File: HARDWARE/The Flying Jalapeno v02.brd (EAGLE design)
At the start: 73.7 x 72.4 mm, 100 parts, among them Q2 MMBT2222A, Q3 NDP6020P, Q4 MMBT2222A, Q5 NDP6020P, Q6 BSS138, 200mA/50V, Q7 BSS138, 200mA/50V, U1 ATMEGA2560AU, U2 LM1117, U3 LM1117, U4 LM1117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

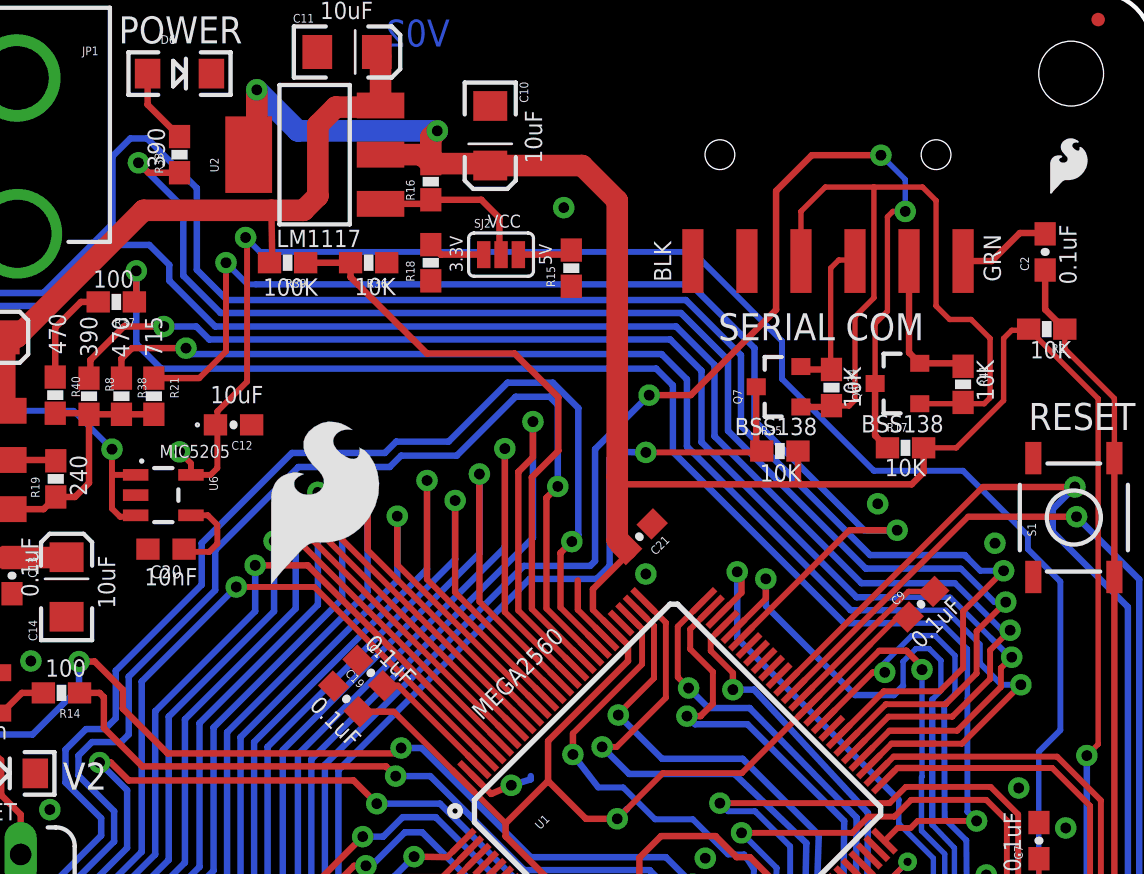
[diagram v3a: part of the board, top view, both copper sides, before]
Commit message: removed RAW split test, moved pwr led from io to VCC
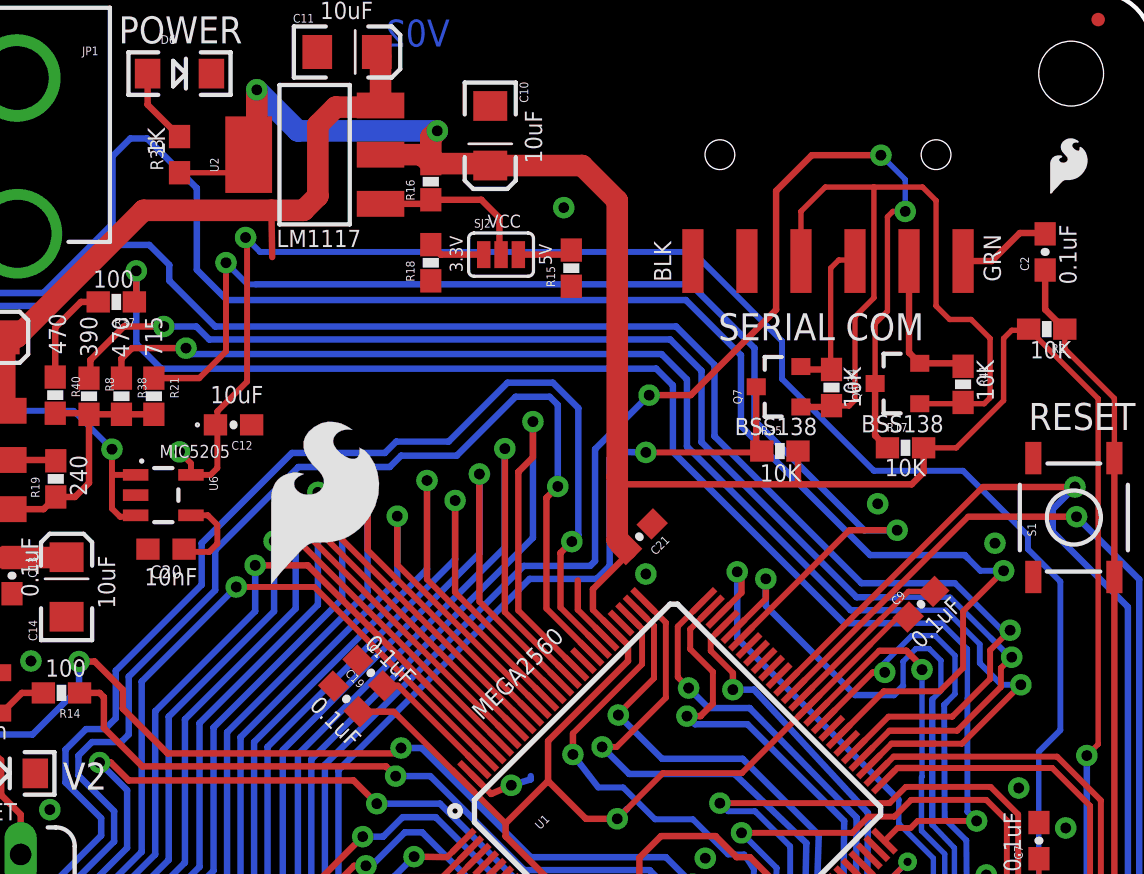
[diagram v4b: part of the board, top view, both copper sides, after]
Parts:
- removed R36: 10K, SparkFun-Resistors:0603-RES
- removed R39: 100k, SparkFun-Resistors:0603-RES
- R33: value 390 -> 1k; device SparkFun-Resistors:0603-RES -> SparkFun-Resistors:0603
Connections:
- removed net 34/RAW_PASS_LED: R33.1, U1.56
- net A13/RAW_READ: no longer R36.2, R39.1
- net GND: no longer R36.1
- net RAW: no longer R39.2
- net VCC: now also R33.1
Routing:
- net 34/RAW_PASS_LED: track 66.7 -> 0.00 mm, vias 2 -> 0
- net A13/RAW_READ: track 28.8 -> 0.00 mm
- net VCC: track 187.9 -> 191.5 mm
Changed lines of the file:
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@@
 <text x="1.6256" y="39.9542" size="0.8128" layer="21" font="vector" ratio="15">10K</text>
 <text x="13.8684" y="40.132" size="0.8128" layer="21" font="vector" ratio="15">10K</text>
-<text x="38.1" y="58.9788" size="0.8128" layer="21" font="vector" ratio="15" rot="R180">10K</text>
 <text x="12.1666" y="40.7416" size="0.8128" layer="21" font="vector" ratio="15" rot="R180">100</text>
 <text x="23.5458" y="41.0464" size="0.8128" layer="21" font="vector" ratio="15" rot="R180">100</text>
@@
 <text x="44.9834" y="64.3636" size="0.8128" layer="21" font="vector" ratio="15" rot="R90">10uF</text>
 <text x="37.0332" y="71.9582" size="0.8128" layer="21" font="vector" ratio="15" rot="R180">10uF</text>
-<text x="34.4424" y="58.9534" size="0.8128" layer="21" font="vector" ratio="15" rot="R180">100K</text>
-<text x="26.4414" y="66.04" size="0.8128" layer="21" font="vector" ratio="15" rot="R270">390</text>
+<text x="26.4414" y="66.04" size="0.8128" layer="21" font="vector" ratio="15" rot="R270">1K</text>
 <text x="36.4744" y="61.2394" size="0.8128" layer="21" font="vector" ratio="15" rot="R180">LM1117</text>
 <text x="6.8326" y="46.609" size="0.8128" layer="21" font="vector" ratio="15" rot="R180">LM1117</text>
@@
 <element name="STANDOFF3" library="SparkFun-Electromechanical" package="STAND-OFF-TIGHT" value="STAND-OFFTIGHT" x="69.85" y="68.58"/>
 <element name="STANDOFF4" library="SparkFun-Electromechanical" package="STAND-OFF-TIGHT" value="STAND-OFFTIGHT" x="3.81" y="68.58"/>
-<element name="R36" library="SparkFun-Resistors" package="0603-RES" value="10K" x="36.83" y="59.69" rot="R180">
-<attribute name="PROD_ID" value="RES-00824" x="36.83" y="59.69" size="1.778" layer="27" font="vector" ratio="15" rot="R180" display="off"/>
-</element>
 <element name="R37" library="SparkFun-Resistors" package="0603-RES" value="100" x="24.9682" y="57.8485" rot="R180">
 <attribute name="PROD_ID" value="RES-07863" x="24.9682" y="57.8485" size="1.778" layer="27" font="vector" ratio="15" rot="R180" display="off"/>
@@
 <attribute name="PROD_ID" value="RES-07869" x="25.2095" y="53.4162" size="1.778" layer="27" font="vector" ratio="15" rot="R270" display="off"/>
 </element>
-<element name="R39" library="SparkFun-Resistors" package="0603-RES" value="100k" x="33.02" y="59.69" rot="R180">
-<attribute name="PROD_ID" value="RES-07828" x="33.02" y="59.69" size="1.778" layer="27" font="vector" ratio="15" rot="R180" display="off"/>
-</element>
 <element name="C19" library="SparkFun-Capacitors" package="0603-CAP" value="0.1uF" x="35.782703125" y="39.187578125" rot="R315">
 <attribute name="PROD_ID" value="CAP-00810" x="35.782703125" y="39.187578125" size="1.778" layer="27" font="vector" ratio="15" rot="R315" display="off"/>
@@
 <attribute name="PROD_ID" value="DIO-00809" x="27.94" y="68.58" size="1.778" layer="27" font="vector" ratio="15" display="off"/>
 </element>
-<element name="R33" library="SparkFun-Resistors" package="0603-RES" value="390" x="27.94" y="64.77" rot="R90">
-<attribute name="PROD_ID" value="RES-07864" x="27.94" y="64.77" size="1.778" layer="27" font="vector" ratio="15" rot="R90" display="off"/>
+<element name="R33" library="SparkFun-Resistors" package="0603" value="1k" x="27.94" y="64.77" rot="R90">
+<attribute name="PROD_ID" value="RES-07856" x="27.94" y="64.77" size="1.778" layer="27" font="vector" ratio="15" rot="R90" display="off"/>
 </element>
 <element name="Q6" library="SparkFun-DiscreteSemi" package="SOT23-3" value="BSS138, 200mA/50V" x="61.7347" y="54.0131" rot="R90">
@@
 <contactref element="JP4" pad="31"/>
 <contactref element="JP4" pad="1"/>
-<contactref element="R36" pad="1"/>
 <contactref element="D3" pad="C"/>
 <contactref element="Y1" pad="2"/>
@@
 <wire x1="63.2714" y1="27.9654" x2="63.2714" y2="25.923240625" width="0.254" layer="1"/>
 <wire x1="63.2714" y1="25.923240625" x2="64.137540625" y2="25.0571" width="0.254" layer="1"/>
+<contactref element="R33" pad="1"/>
+<wire x1="31.191" y1="64.77" x2="30.341" y2="63.92" width="0.254" layer="1"/>
+<wire x1="30.341" y1="63.92" x2="27.94" y2="63.92" width="0.254" layer="1"/>
 </signal>
 <signal name="RAW" class="1">
@@
 <contactref element="SJ3" pad="1"/>
 <contactref element="SJ4" pad="1"/>
-<contactref element="R39" pad="2"/>
 <wire x1="2.032" y1="58.036" x2="4.448" y2="58.036" width="1.016" layer="1"/>
 <wire x1="4.448" y1="58.036" x2="5.6769" y2="56.8071" width="1.016" layer="1"/>
@@
 <via x="16.0909" y="52.7304" extent="1-16" drill="0.508"/>
 <wire x1="16.0909" y1="52.7304" x2="19.6342" y2="52.7304" width="1.016" layer="1"/>
-<wire x1="32.17" y1="59.69" x2="32.297" y2="59.9558" width="0.3048" layer="1"/>
 <wire x1="32.297" y1="59.9558" x2="32.258" y2="62.1538" width="0.3048" layer="1"/>
 <wire x1="3.8354" y1="45.5676" x2="3.8354" y2="44.2468" width="1.016" layer="1"/>
@@
 <signal name="A13/RAW_READ">
 <contactref element="U1" pad="84"/>
-<contactref element="R36" pad="2"/>
-<contactref element="R39" pad="1"/>
-<wire x1="35.98" y1="59.69" x2="33.87" y2="59.69" width="0.3048" layer="1"/>
-<wire x1="46.929328125" y1="40.989090625" x2="44.5008" y2="43.41761875" width="0.2794" layer="1"/>
-<wire x1="44.5008" y1="43.41761875" x2="44.5008" y2="49.6062" width="0.3048" layer="1"/>
-<wire x1="44.5008" y1="49.6062" x2="45.7454" y2="50.8508" width="0.3048" layer="1"/>
-<wire x1="45.7454" y1="50.8508" x2="45.7454" y2="53.3654" width="0.3048" layer="1"/>
-<wire x1="45.7454" y1="53.3654" x2="43.688" y2="55.4228" width="0.3048" layer="1"/>
-<wire x1="43.688" y1="55.4228" x2="39.5732" y2="55.4228" width="0.3048" layer="1"/>
-<wire x1="39.5732" y1="55.4228" x2="35.98" y2="59.016" width="0.3048" layer="1"/>
-<wire x1="35.98" y1="59.016" x2="35.98" y2="59.69" width="0.3048" layer="1"/>
 </signal>
 <signal name="A12">
@@
 <wire x1="66.5988" y1="42.418" x2="66.9798" y2="42.418" width="0.2794" layer="16"/>
 </signal>
-<signal name="34/RAW_PASS_LED">
-<contactref element="U1" pad="56"/>
-<contactref element="R33" pad="1"/>
-<wire x1="59.303696875" y1="37.100003125" x2="61.14189375" y2="38.9382" width="0.2794" layer="1"/>
-<via x="66.7766" y="43.7388" extent="1-16" drill="0.508"/>
-<wire x1="64.6176" y1="45.3136" x2="60.198" y2="45.3136" width="0.3048" layer="16"/>
-<wire x1="60.198" y1="45.3136" x2="53.721" y2="51.7906" width="0.3048" layer="16"/>
-<wire x1="53.721" y1="51.7906" x2="53.721" y2="55.118" width="0.3048" layer="16"/>
-<wire x1="53.721" y1="55.118" x2="51.5112" y2="57.3278" width="0.3048" layer="16"/>
-<wire x1="51.5112" y1="57.3278" x2="29.8704" y2="57.3278" width="0.3048" layer="16"/>
-<wire x1="29.8704" y1="57.3278" x2="28.1178" y2="59.0804" width="0.3048" layer="16"/>
-<wire x1="28.1178" y1="59.0804" x2="28.1178" y2="62.2808" width="0.3048" layer="16"/>
-<wire x1="28.1178" y1="62.2808" x2="26.0096" y2="64.389" width="0.3048" layer="16"/>
-<via x="26.0096" y="64.389" extent="1-16" drill="0.508"/>
-<wire x1="26.0096" y1="64.389" x2="26.4786" y2="63.92" width="0.3048" layer="1"/>
-<wire x1="26.4786" y1="63.92" x2="27.94" y2="63.92" width="0.3048" layer="1"/>
-<wire x1="61.14189375" y1="38.9382" x2="63.9572" y2="38.9382" width="0.2794" layer="1"/>
-<wire x1="63.9572" y1="38.9382" x2="65.405" y2="40.386" width="0.2794" layer="1"/>
-<wire x1="65.405" y1="40.386" x2="65.405" y2="42.3672" width="0.2794" layer="1"/>
-<wire x1="65.405" y1="42.3672" x2="66.7766" y2="43.7388" width="0.2794" layer="1"/>
-<wire x1="64.6176" y1="45.3136" x2="64.6684" y2="45.3136" width="0.2794" layer="16"/>
-<wire x1="64.6684" y1="45.3136" x2="66.2432" y2="43.7388" width="0.2794" layer="16"/>
-<wire x1="66.2432" y1="43.7388" x2="66.7766" y2="43.7388" width="0.2794" layer="16"/>
-</signal>
 <signal name="33/V1_3.3V">
